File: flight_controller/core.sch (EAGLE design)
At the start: 116 parts, among them J1 MOLEX-2POS, J10 MOLEX-2POS, J11 MOLEX-2POS, J12 MOLEX-2POS, J13 MOLEX-3POS, J14 MOLEX-3POS, J15 MOLEX-4POS, J16 MOLEX-3POS, J17 MOLEX-3POS, J18 MOLEX-4POS, J19 MOLEX-3POS, J2 MOLEX-2POS, J20 MOLEX-4POS, J3 MOLEX-2POS, J4 MOLEX-2POS, J5 MOLEX-2POS, J6 MOLEX-2POS, J7 MOLEX-2POS, J8 MOLEX-2POS, J9 MOLEX-2POS, Q1 MMBT2222A, Q14 MMBT2222A, Q15 MMBT2222A, Q16 MMBT2222A, Q17 MMBT2222A, Q3 MMBT2222A, Q4 MMBT2222A, Q9 MMBT2222A, U1 MPU-6000QFN-24, U2 MEAS-MS5611, U3 USD-SOCKETNEW, U4 STM32F405, U5 MIC5219 3.3V

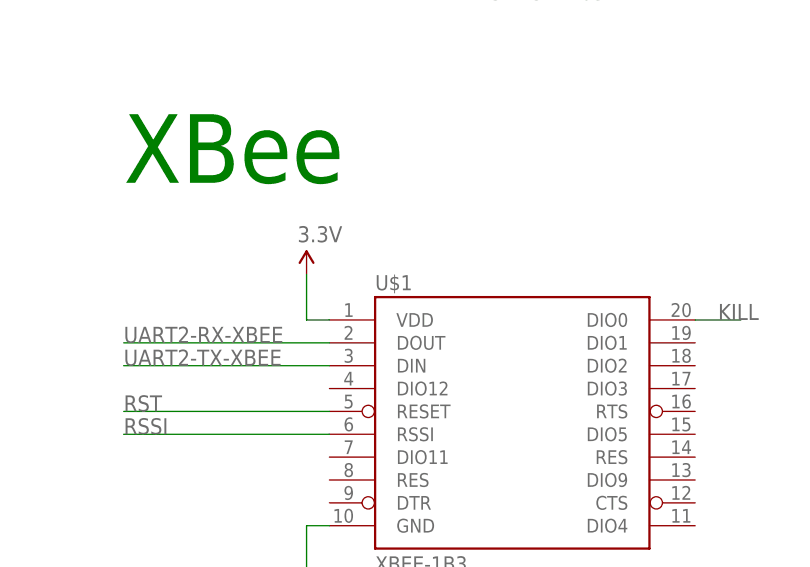
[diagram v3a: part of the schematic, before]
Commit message: Explicitly name XBee package.
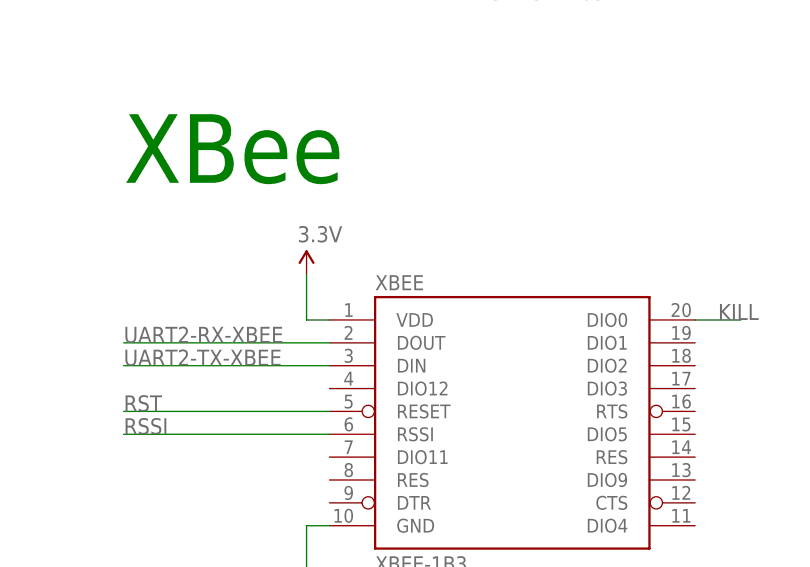
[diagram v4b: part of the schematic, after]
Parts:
- renumbered U$1 to XBEE
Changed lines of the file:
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@@
 <part name="C16" library="SparkFun-Capacitors" deviceset="18PF-50V-5%(0603)" device="" value="18pF"/>
 <part name="GND26" library="SparkFun-Aesthetics" deviceset="GND" device=""/>
-<part name="U$1" library="SparkFun-RF" deviceset="XBEE-1" device="B3"/>
+<part name="XBEE" library="SparkFun-RF" deviceset="XBEE-1" device="B3"/>
 <part name="GND27" library="SparkFun-Aesthetics" deviceset="GND" device=""/>
 <part name="SUPPLY11" library="SparkFun-Aesthetics" deviceset="3.3V" device=""/>
@@
 <instance part="C16" gate="G$1" x="111.76" y="185.42" rot="R90"/>
 <instance part="GND26" gate="1" x="116.84" y="180.34"/>
-<instance part="U$1" gate="G$1" x="58.42" y="111.76"/>
+<instance part="XBEE" gate="G$1" x="58.42" y="111.76"/>
 <instance part="GND27" gate="1" x="35.56" y="91.44"/>
 <instance part="SUPPLY11" gate="G$1" x="35.56" y="127"/>
@@
 </segment>
 <segment>
-<pinref part="U$1" gate="G$1" pin="GND"/>
+<pinref part="XBEE" gate="G$1" pin="GND"/>
 <wire x1="38.1" y1="99.06" x2="35.56" y2="99.06" width="0.1524" layer="91"/>
 <wire x1="35.56" y1="99.06" x2="35.56" y2="93.98" width="0.1524" layer="91"/>
@@
 </segment>
 <segment>
-<pinref part="U$1" gate="G$1" pin="RESET"/>
+<pinref part="XBEE" gate="G$1" pin="RESET"/>
 <wire x1="38.1" y1="111.76" x2="15.24" y2="111.76" width="0.1524" layer="91"/>
 <label x="15.24" y="111.76" size="1.778" layer="95"/>
@@
 </segment>
 <segment>
-<pinref part="U$1" gate="G$1" pin="VDD"/>
+<pinref part="XBEE" gate="G$1" pin="VDD"/>
 <wire x1="38.1" y1="121.92" x2="35.56" y2="121.92" width="0.1524" layer="91"/>
 <wire x1="35.56" y1="121.92" x2="35.56" y2="127" width="0.1524" layer="91"/>
@@
 <wire x1="83.82" y1="121.92" x2="78.74" y2="121.92" width="0.1524" layer="91"/>
 <label x="81.28" y="121.92" size="1.778" layer="95"/>
-<pinref part="U$1" gate="G$1" pin="DIO0"/>
+<pinref part="XBEE" gate="G$1" pin="DIO0"/>
 </segment>
 </net>
@@
 </segment>
 <segment>
-<pinref part="U$1" gate="G$1" pin="RSSI"/>
+<pinref part="XBEE" gate="G$1" pin="RSSI"/>
 <wire x1="38.1" y1="109.22" x2="15.24" y2="109.22" width="0.1524" layer="91"/>
 <label x="15.24" y="109.22" size="1.778" layer="95"/>
@@
 </segment>
 <segment>
-<pinref part="U$1" gate="G$1" pin="DIN"/>
+<pinref part="XBEE" gate="G$1" pin="DIN"/>
 <wire x1="38.1" y1="116.84" x2="15.24" y2="116.84" width="0.1524" layer="91"/>
 <label x="15.24" y="116.84" size="1.778" layer="95"/>
@@
 </segment>
 <segment>
-<pinref part="U$1" gate="G$1" pin="DOUT"/>
+<pinref part="XBEE" gate="G$1" pin="DOUT"/>
 <wire x1="38.1" y1="119.38" x2="15.24" y2="119.38" width="0.1524" layer="91"/>
 <label x="15.24" y="119.38" size="1.778" layer="95"/>

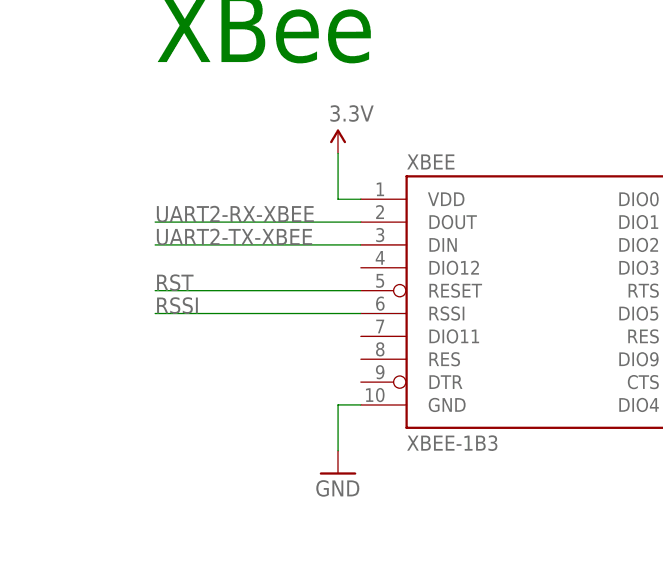
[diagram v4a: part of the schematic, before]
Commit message: Remove XBee reset pin from global reset net.
The XBee pin is for factory resetting the device! Read the datasheet, people!
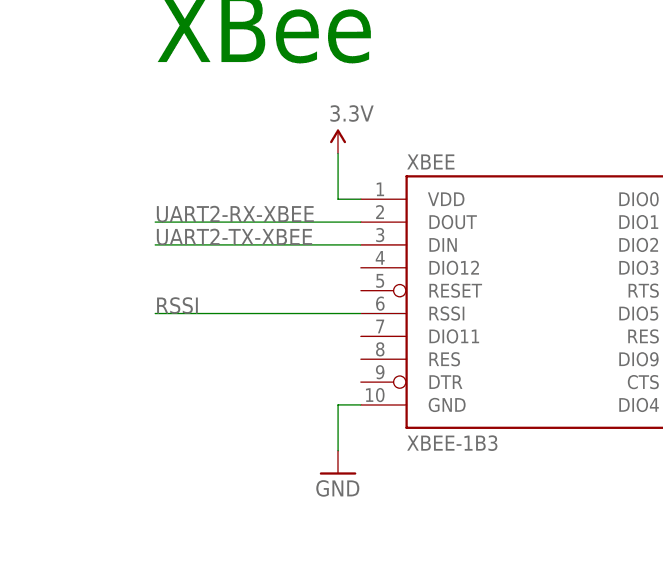
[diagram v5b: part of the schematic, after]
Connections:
- net RST: no longer XBEE.RESET
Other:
- note removed: "TODO(yoos): Why is RST on XBee reset?"
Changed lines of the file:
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@@
 <text x="15.24" y="172.72" size="1.778" layer="98">AF UART3</text>
 <text x="104.14" y="236.22" size="1.778" layer="98">AF ADC</text>
-<text x="213.36" y="-429.26" size="1.778" layer="98">TODO(yoos): Why is RST on XBee reset?</text>
 <text x="266.7" y="-464.82" size="7.62" layer="91">uSD</text>
 <text x="0" y="-375.92" size="12.7" layer="91">CONNECTORS/BUSES</text>
@@
 <pinref part="U4" gate=".GPIO" pin="NRST"/>
 </segment>
-<segment>
-<pinref part="XBEE" gate="G$1" pin="RESET"/>
-<wire x1="38.1" y1="111.76" x2="15.24" y2="111.76" width="0.1524" layer="91"/>
-<label x="15.24" y="111.76" size="1.778" layer="95"/>
-</segment>
 </net>

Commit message: Add RGB status LED pair.
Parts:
- removed J10, J11, J12: MOLEX-2POS, aerial:MOLEX-2POS
- removed LED16, LED17, LED18, LED19, LED20, LED21: GREEN, SparkFun-LED:LED0603
- removed R35, R36: 680, SparkFun-Passives:RESISTOR0603-RES
- added Q2, Q5, Q6: 200mA/50V, SparkFun-DiscreteSemi:MOSFET-NCHANNELBSS138
- LED14, LED15: value GREEN -> OSRAM-MULTILED-RGB; device SparkFun-LED:LED0603 -> aerial:OSRAM-MULTILED-RGB
- R10, R26: value 680 -> 120
- R24, R25, R33, R34: value 680 -> 100
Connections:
- net TIM3-CH1-K renamed TIM4-CH1-K
- net TIM3-CH2-K renamed TIM4-CH2-K
- net TIM3-CH3-K renamed TIM4-CH3-K
- net TIM3-CH4-K renamed TIM4-CH4-K
- removed net N$31: LED5.A, R24.2
- removed net N$32: LED6.A, R25.2
- removed net N$33: LED7.A, R26.2
- removed net N$40: LED14.A, R33.2
- removed net N$41: LED15.A, R34.2
- removed net N$42: LED16.A, R35.2
- removed net N$43: LED17.A, R36.2
- removed net RSSI: R27.1, XBEE.RSSI
- removed net TIM3-CH2: R10.1, R40.1, U4.GPIO.PA7
- removed net TIM3-CH3: R3.1, R41.1, U4.GPIO.PB0
- removed net TIM3-CH4: R4.1, R42.1, U4.GPIO.PB1
- new net N$12: LED14.B+, R25.2
- new net N$19: LED15.B+, R34.2
- new net N$3: LED6.A, R4.2
- new net N$5: LED14.B-, LED15.B-, Q2.D
- new net N$6: LED14.G-, LED15.G-, Q5.D
- new net N$7: LED14.R-, LED15.R-, Q6.D
- new net N$8: LED14.R+, R10.2
- new net N$9: LED14.G+, R24.2
- new net TIM3-CH1-RSSI: R27.1, U4.GPIO.PA6, XBEE.RSSI
- new net TIM3-CH2-STSB: Q2.G
- new net TIM3-CH2-STSR: U4.GPIO.PA7
- new net TIM3-CH3-STSG: Q5.G, U4.GPIO.PB0
- new net TIM3-CH4-STSB: U4.GPIO.PB1
- new net TIM3-CH4-STSR: Q6.G
- net 5V: now also R10.1, R24.1, R25.1, R26.1, R33.1, R34.1
- net GND: now also Q2.S, Q5.S, Q6.S; no longer J10.2, J11.2, J12.2, LED14.C, LED15.C, LED16.C, LED17.C, LED18.C, LED19.C, LED20.C, LED21.C
- net N$15: now also LED15.R+, R26.2; no longer LED20.A, R7.2
- net N$16: now also LED15.G+, R33.2; no longer LED21.A, R10.2
- net N$2: now also LED5.A; no longer LED18.A
- net N$4: now also LED7.A, R7.2; no longer LED19.A, R4.2
- net PA12: now also R3.1; no longer R25.1
- net PA15: now also R4.1; no longer R26.1
- net PB2: now also R7.1; no longer R24.1
- net TIM1-CH1: no longer R35.1
- net TIM1-CH2: no longer R36.1
- net TIM1-CH3: no longer R33.1
- net TIM1-CH4: no longer R34.1
- net TIM3-CH1: now also J9.1; no longer R39.1, R7.1, U4.GPIO.PA6
- net TIM4-CH1: now also R39.1; no longer J9.1
- net TIM4-CH2: now also R40.1; no longer J10.1
- net TIM4-CH3: now also R41.1; no longer J11.1
- net TIM4-CH4: now also R42.1; no longer J12.1
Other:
- note added: "Status LED"
- moved on the sheet: C12, C19, LED1, LED10, LED11, LED12, LED13, LED2, LED3, LED4, LED5, LED6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

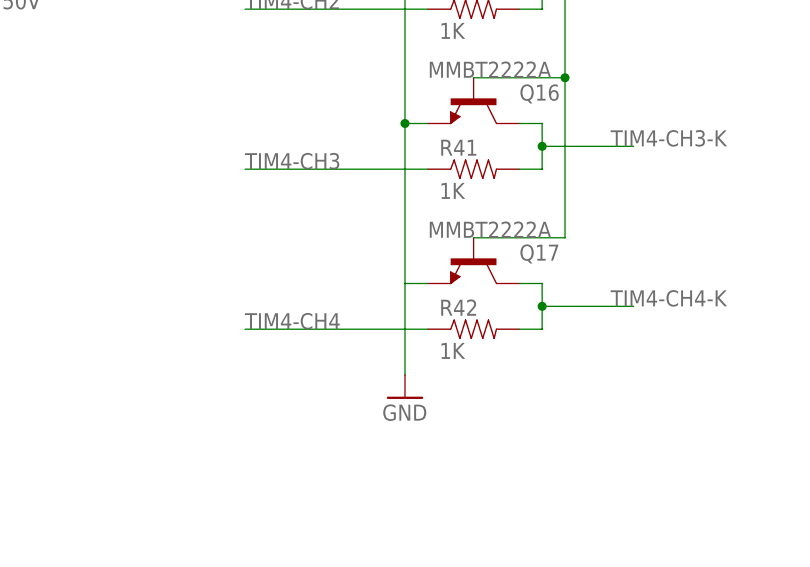
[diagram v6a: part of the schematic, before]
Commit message: Replace components to those from new OSURC libraries.
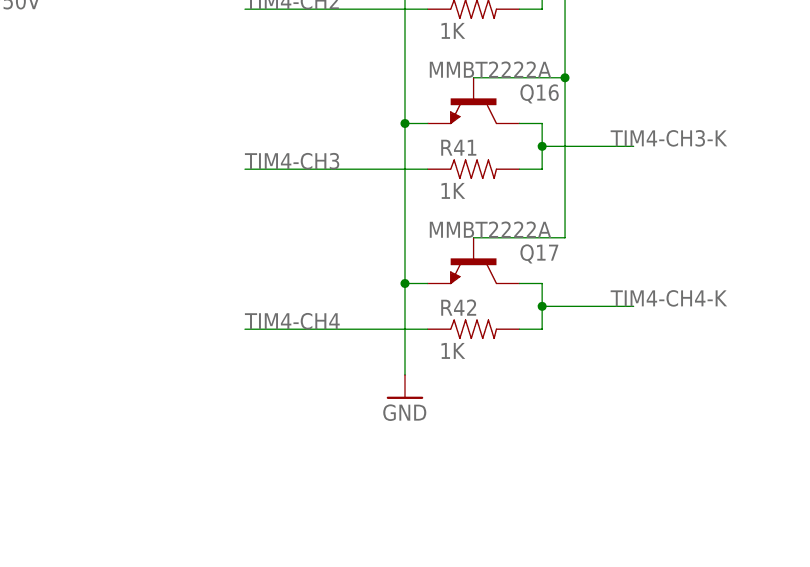
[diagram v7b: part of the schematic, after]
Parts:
- J1: device aerial:MOLEX-2POS -> OSURC_Connectors:MOLEX-2POS
- J17: device aerial:MOLEX-3POS -> OSURC_Connectors:MOLEX-3POS
- J18: device aerial:MOLEX-4POS -> OSURC_Connectors:MOLEX-4POS
- LED14: device aerial:OSRAM-MULTILED-RGB -> OSURC_LED:OSRAM-MULTILED-RGB
- U2: device aerial:MEAS-MS5611 -> OSURC_Sensors:MEAS-MS5611
- U4: device aerial:STM32F405 -> OSURC_DigitalIC:STM32F405
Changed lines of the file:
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@@
 <part name="GND7" library="SparkFun-Aesthetics" deviceset="GND" device=""/>
 <part name="U3" library="SparkFun-Connectors" deviceset="USD-SOCKET" device="NEW"/>
-<part name="U4" library="aerial" deviceset="STM32F405" device=""/>
+<part name="U4" library="OSURC_DigitalIC" deviceset="STM32F405" device=""/>
 <part name="R8" library="SparkFun" deviceset="RESISTOR" device="0603-RES" value="20K"/>
 <part name="C8" library="SparkFun-Capacitors" deviceset="0.1UF-25V-5%(0603)" device="" value="0.1uF"/>
@@
 <part name="GND15" library="SparkFun-Aesthetics" deviceset="GND" device=""/>
 <part name="GND16" library="SparkFun-Aesthetics" deviceset="GND" device=""/>
-<part name="J1" library="aerial" deviceset="MOLEX-2POS" device=""/>
+<part name="J1" library="OSURC_Connectors" deviceset="MOLEX-2POS" device=""/>
 <part name="J2" library="aerial" deviceset="MOLEX-2POS" device=""/>
 <part name="J3" library="aerial" deviceset="MOLEX-2POS" device=""/>
@@
 <part name="J14" library="aerial" deviceset="MOLEX-3POS" device=""/>
 <part name="J16" library="aerial" deviceset="MOLEX-3POS" device=""/>
-<part name="J17" library="aerial" deviceset="MOLEX-3POS" device=""/>
+<part name="J17" library="OSURC_Connectors" deviceset="MOLEX-3POS" device=""/>
 <part name="J19" library="aerial" deviceset="MOLEX-3POS" device=""/>
 <part name="J20" library="aerial" deviceset="MOLEX-4POS" device=""/>
@@
 <part name="C10" library="SparkFun-Capacitors" deviceset="2.2UF-10V-20%(0603)" device="" value="2.2uF"/>
 <part name="C13" library="SparkFun-Capacitors" deviceset="2.2UF-10V-20%(0603)" device="" value="2.2uF"/>
-<part name="U2" library="aerial" deviceset="MEAS-MS5611" device=""/>
+<part name="U2" library="OSURC_Sensors" deviceset="MEAS-MS5611" device=""/>
 <part name="GND23" library="SparkFun-Aesthetics" deviceset="GND" device=""/>
 <part name="SUPPLY9" library="SparkFun-Aesthetics" deviceset="3.3V" device=""/>
@@
 <part name="GND27" library="SparkFun-Aesthetics" deviceset="GND" device=""/>
 <part name="SUPPLY11" library="SparkFun-Aesthetics" deviceset="3.3V" device=""/>
-<part name="J18" library="aerial" deviceset="MOLEX-4POS" device=""/>
+<part name="J18" library="OSURC_Connectors" deviceset="MOLEX-4POS" device=""/>
 <part name="GND3" library="SparkFun-Aesthetics" deviceset="GND" device=""/>
 <part name="SUPPLY3" library="SparkFun-Aesthetics" deviceset="5V" device=""/>
@@
 <part name="LED6" library="SparkFun-LED" deviceset="LED" device="0603" value="ORANGE"/>
 <part name="LED7" library="SparkFun-LED" deviceset="LED" device="0603" value="ORANGE"/>
-<part name="LED14" library="aerial" deviceset="OSRAM-MULTILED-RGB" device=""/>
+<part name="LED14" library="OSURC_LED" deviceset="OSRAM-MULTILED-RGB" device=""/>
 <part name="Q2" library="SparkFun-DiscreteSemi" deviceset="MOSFET-NCHANNEL" device="BSS138" value="200mA/50V"/>
 <part name="Q5" library="SparkFun-DiscreteSemi" deviceset="MOSFET-NCHANNEL" device="BSS138" value="200mA/50V"/>
@@
 <text x="259.08" y="-523.24" size="7.62" layer="98">TODO</text>
 <text x="246.38" y="243.84" size="5.08" layer="91">Status LED</text>
-<text x="345.44" y="81.28" size="12.7" layer="98">TODO</text>
+<text x="411.48" y="119.38" size="12.7" layer="98">TODO</text>
 </plain>
 <instances>
@@
 <wire x1="363.22" y1="116.84" x2="363.22" y2="106.68" width="0.1524" layer="91"/>
 <pinref part="GND9" gate="1" pin="GND"/>
-</segment>
-<segment>
+<junction x="363.22" y="116.84"/>
+</segment>
+<segment>
